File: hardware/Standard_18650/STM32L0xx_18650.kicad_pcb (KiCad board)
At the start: 2 copper layers, 109.7 x 16 mm, 54 parts, among them J2 Battery, J3 GPIO, J4 USB_B_Micro, J5 Power, J6 LEDs, J7 GPIO, Q1 BSS806N, Q2 BSS806N, Q3 BSS806N, Q4 BSS806N, SW1 Mode, SW2 Power, U1 STM32L072KZTx, U2 AP2210N-3.3TRG1, U3 BQ21040, U4 ESD7002WTT1G, Y1 32.768kHz

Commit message: Minor adjustments/text/icon
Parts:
- removed the REF** at (146.6, 99.9)
- added REF**: OSHW-Symbol_6.7x6mm_Copper, Symbol:OSHW-Symbol_6.7x6mm_Copper, B.Cu at (146.6, 100.0)
- C1: value 0.1uF -> 100nF
- C13, C6: value 1.0uf -> 1uf
- R11: value 430 -> 330
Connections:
- J4 pad 4: (no net) -> Net-(J4-Pad4)
- U1 pad 14: (no net) -> Net-(U1-Pad14)
- U1 pad 15: (no net) -> Net-(U1-Pad15)
- U1 pad 25: (no net) -> Net-(U1-Pad25)
- U1 pad 26: (no net) -> Net-(U1-Pad26)
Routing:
- net +BATT: track 80.6 -> 94.4 mm

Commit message: Rename SCLK to SCK
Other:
- board text added: "SCK"
- board text removed: "SCLK"
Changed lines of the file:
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@@
     (effects (font (size 0.65 0.6) (thickness 0.1)) (justify mirror))
   )
-  (gr_text SCLK (at 82.2 93.6) (layer B.SilkS)
+  (gr_text SCK (at 82.2 93.6) (layer B.SilkS)
     (effects (font (size 0.65 0.6) (thickness 0.1)) (justify mirror))
   )

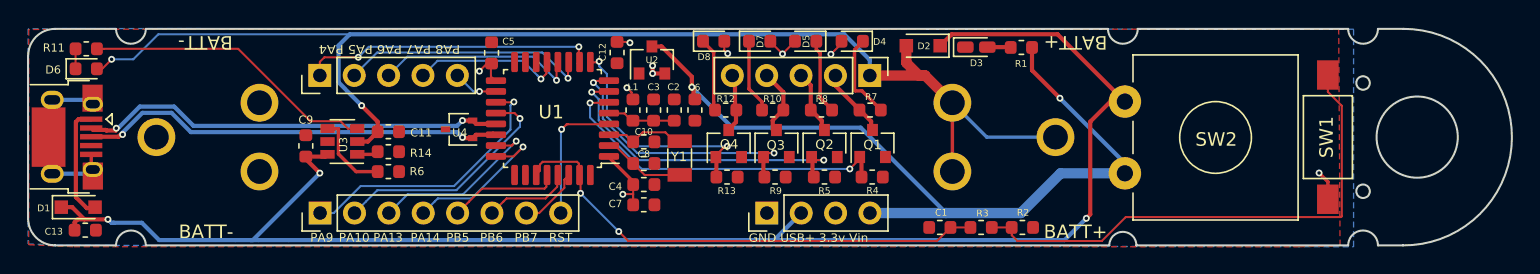
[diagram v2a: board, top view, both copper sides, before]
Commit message: Use STM32F412CGUx (Regular & Tiny)
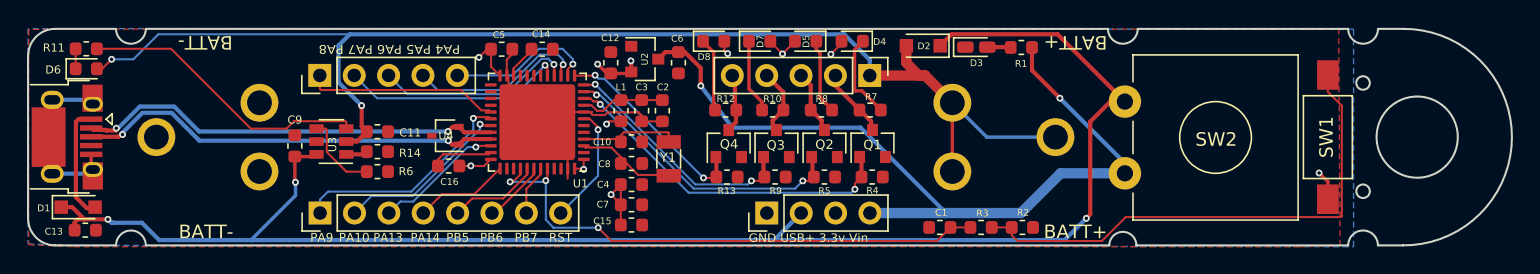
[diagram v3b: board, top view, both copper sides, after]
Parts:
- added C14: 4.7uF, Capacitor_SMD:C_0603_1608Metric, F.Cu at (96.1, 93.5)
- added C15: 100nf, Capacitor_SMD:C_0603_1608Metric, F.Cu at (102.7, 106.5)
- added C16: 100nf, Capacitor_SMD:C_0603_1608Metric, F.Cu at (89.2, 102.1)
- C3: value 10nf -> 100nf
- U1: value STM32L072KZTx -> STM32F412CGUx; footprint Package_QFP:LQFP-32_7x7mm_P0.8mm -> Package_DFN_QFN:QFN-48-1EP_7x7mm_P0.5mm_EP5.6x5.6mm
- moved C6 3.70 mm to (106.2, 94.5)
- moved U1 1.15 mm to (95.7, 98.9)
- moved U4 1.11 mm to (88.9, 99.9)
- moved C10 0.91 mm to (102.7, 100.3)
- moved C4 0.91 mm to (102.7, 103.5)
- moved C7 0.91 mm to (102.7, 105.0)
- moved C8 0.91 mm to (102.7, 102.0)
- moved C12 0.89 mm to (101.2, 94.5), turned to 90 degrees
- moved C3 0.88 mm to (103.4, 98.0), turned to 270 degrees
- moved C2 0.88 mm to (105.0, 98.0), turned to 270 degrees
- moved L1 0.88 mm to (101.9, 98.0), turned to 270 degrees
- moved Y1 0.81 mm to (105.4, 101.6)
- moved C9 0.81 mm to (77.8, 100.7)
- moved U3 0.81 mm to (80.5, 100.3)
- moved C11 0.81 mm to (83.9, 99.6)
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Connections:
- C10 pad 1: Net-(C10-Pad1) -> /XTAL2
- C2 pad 1: Net-(C2-Pad1) -> /VDDA
- C3 pad 1: Net-(C2-Pad1) -> /VDDA
- C8 pad 1: Net-(C8-Pad1) -> /XTAL1
- J3 pad 1: /PA4 -> /PA8
- J3 pad 2: /PA5 -> /PA7
- J3 pad 4: /PA7 -> /PA5
- J3 pad 5: /PA8 -> /PA4
- J4 pad 4: Net-(J4-Pad4) -> (no net)
- L1 pad 1: Net-(C2-Pad1) -> /VDDA
- U1 pad 10: /PA4 -> /LED1
- U1 pad 11: /PA5 -> /LED2
- U1 pad 12: /PA6 -> /LED3
- U1 pad 13: /PA7 -> /LED4
- U1 pad 14: Net-(U1-Pad14) -> /PA4
- U1 pad 15: Net-(U1-Pad15) -> /PA5
- U1 pad 16: GND -> /PA6
- U1 pad 17: +3V3 -> /PA7
- U1 pad 18: /PA8 -> (no net)
- U1 pad 19: /PA9 -> (no net)
- U1 pad 2: Net-(C8-Pad1) -> (no net)
- U1 pad 20: /PA10 -> (no net)
- U1 pad 21: /USB_D- -> (no net)
- U1 pad 22: /USB_D+ -> Net-(C14-Pad1)
- U1 pad 23: /PA13 -> GND
- U1 pad 24: /PA14 -> +3V3
- U1 pad 25: Net-(U1-Pad25) -> (no net)
- U1 pad 26: Net-(U1-Pad26) -> (no net)
- U1 pad 27: /BUTTON -> (no net)
- U1 pad 28: /PB5 -> (no net)
- U1 pad 29: /PB6 -> /PA8
- U1 pad 3: Net-(C10-Pad1) -> /XTAL1
- U1 pad 30: /PB7 -> /PA9
- U1 pad 31: /BUTTON -> /PA10
- U1 pad 32: GND -> /USB_D-
- U1 pad 4: /RESET -> /XTAL2
- U1 pad 5: Net-(C2-Pad1) -> (no net)
- U1 pad 6: /LED1 -> (no net)
- U1 pad 7: /LED2 -> /RESET
- U1 pad 8: /LED3 -> GND
- U1 pad 9: /LED4 -> /VDDA
- Y1 pad 1: Net-(C8-Pad1) -> /XTAL1
- Y1 pad 2: Net-(C10-Pad1) -> /XTAL2
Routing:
- net GND: track 7.43 -> 31.8 mm
- net /PA8: track 3.36 -> 14.3 mm, vias 1 -> 0
- net /PA4: track 21.9 -> 11.0 mm, vias 2 -> 1
- net /XTAL2: track 0.00 -> 7.61 mm
- net /XTAL1: track 0.00 -> 7.45 mm
- net +3V3: track 18.0 -> 24.4 mm, vias 10 -> 11
- net /VDDA: track 0.00 -> 6.31 mm
- net Net-(C8-Pad1): track 6.18 -> 0.00 mm
- net Net-(C10-Pad1): track 6.04 -> 0.00 mm
- net /PA7: track 11.1 -> 16.7 mm
- net /PA5: track 18.5 -> 13.3 mm
- net Net-(C2-Pad1): track 4.95 -> 0.00 mm
- net /PA14: track 11.7 -> 7.03 mm, vias 1 -> 0
- net /PA10: track 17.4 -> 13.0 mm
- net /PA13: track 13.3 -> 9.58 mm
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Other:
- board text added: "PA4 PA5 PA6 PA7 PA8"
- board text added: "rev 1.1a"
- board text removed: "PA8 PA7 PA6 PA5 PA4"
- board text removed: "rev 1"
